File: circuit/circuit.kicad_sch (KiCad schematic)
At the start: 23 parts, among them SW101 SW_Push, SW102 SW_Push, SW103 SW_Push, SW104 SW_Push, SW105 SW_Push, SW106 SW_Push, SW107 SW_Push, SW108 SW_Push, SW109 SW_Push, SW110 SW_Push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

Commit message: Hopefully close to finished
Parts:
- removed U5: ESP32-S3-DevKitC, Esp32 DevKits:ESP32-S3-DevKitC, symbol PCM_Espressif:ESP32-S3-DevKitC
- added U5: ESP32-S3-DevKitC, ESP:ESP32-S3-DevKitC, symbol Espressif:ESP32-S3-DevKitC
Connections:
- net +5V: now also U5.21 (5V)
- net 3.3V: now also U5.1 (3V3), U5.2 (3V3)
- net GND: now also U5.22 (GND), U5.23 (GND), U5.24 (GND), U5.44 (GND)
- net SR_DS: now also U5.9 (GPIO16/ADC2_CH5/32K_N)
- net SR_OE: now also U5.25 (GPIO19/USB_D-)
- net SR_SHCP: now also U5.10 (GPIO17/ADC2_CH6)
- net SR_STCP: now also U5.11 (GPIO18/ADC2_CH7)
- net at C103.2, SW103.1: now also U5.12 (GPIO8/ADC1_CH7)
- net at C105.2, SW105.1: now also U5.16 (GPIO10/ADC1_CH9)
- net at C107.2, SW107.1: now also U5.18 (GPIO12/ADC2_CH1)
- net at Disp101.2 (SDA): now also U5.4 (GPIO4/ADC1_CH3)
- net at Disp101.3 (SCL): now also U5.5 (GPIO5/ADC1_CH4)
- net at C106.2, SW106.1: now also U5.17 (GPIO11/ADC2_CH0)
- net at C109.2, SW109.1: now also U5.20 (GPIO14/ADC2_CH3)
- net at C102.2, SW102.1: now also U5.7 (GPIO7/ADC1_CH6)
- net at C108.2, SW108.1: now also U5.19 (GPIO13/ADC2_CH2)
- net at C110.2, SW110.1: now also U5.8 (GPIO15/ADC2_CH4/32K_P)
- net at C104.2, SW104.1: now also U5.15 (GPIO9/ADC1_CH8)
- net at C101.2, SW101.1: now also U5.6 (GPIO6/ADC1_CH5)
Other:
- sheet IO Routing ports: added none; removed U10_Q[0..5]
- sheet Pedal Routing 1 - 4 ports: added U9_Q[0..7]; removed U7_Q[0..7]
- sheet Pedal Routing 5 - 8 ports: added U10_Q[0..7]; removed U10_Q[0..5], U8_Q[0..7]
- sheet Shift Registers ports: added U10_Q[0..7]; removed U10_Q[0..5]

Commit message: Created pdf and made minor readabilty changes.
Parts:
- C101, C102, C103, C104, C105, C106, C107, C108, C109, C110: value 0.1mF -> .1uF
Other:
- sheet IO Routing: file iorouting.kicad_sch -> io_routing.kicad_sch
- sheet Pedal Routing 5 - 8: file pedal_routing_4-8.kicad_sch -> pedal_routing_5-8.kicad_sch
- title: (none) -> ESP332 Guitar Patch Bay
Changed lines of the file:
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@@
 	(generator "eeschema")
 	(generator_version "9.0")
-	(paper "A2")
+	(paper "USLetter")
+	(title_block
+		(title "ESP332 Guitar Patch Bay")
+		(date "2025-05-27")
+		(rev "1")
+	)
 	(junction
 		(at 349.25 114.3)
@@
 	)
 	(junction
+		(at 375.92 38.1)
+		(diameter 0)
+		(color 0 0 0 0)
+	)
+	(junction
 		(at 386.08 38.1)
 		(diameter 0)
@@
 			)
 		)
-		(property "Value" "0.1mF"
+		(property "Value" ".1uF"
 			(at 330.1936 106.68 90)
 			(effects
@@
 			)
 		)
-		(property "Value" "0.1mF"
+		(property "Value" ".1uF"
 			(at 292.0936 132.08 90)
 			(effects
@@
 			)
 		)
-		(property "Value" "0.1mF"
+		(property "Value" ".1uF"
 			(at 279.3936 119.38 90)
 			(effects
@@
 			)
 		)
-		(property "Value" "0.1mF"
+		(property "Value" ".1uF"
 			(at 304.7936 81.28 90)
 			(effects
@@
 			)
 		)
-		(property "Value" "0.1mF"
+		(property "Value" ".1uF"
 			(at 317.4936 157.48 90)
 			(effects
@@
 			)
 		)
-		(property "Value" "0.1mF"
+		(property "Value" ".1uF"
 			(at 304.7936 144.78 90)
 			(effects
@@
 			)
 		)
-		(property "Value" "0.1mF"
+		(property "Value" ".1uF"
 			(at 330.1936 170.18 90)
 			(effects
@@
 	)
 	(symbol
+		(lib_id "power:PWR_FLAG")
+		(at 375.92 38.1 90)
+		(unit 1)
+		(exclude_from_sim no)
+		(in_bom yes)
+		(on_board yes)
+		(dnp no)
+		(fields_autoplaced yes)
+		(property "Reference" "#FLG0102"
+			(at 374.015 38.1 0)
+			(effects
+				(font
+					(size 1.27 1.27)
+				)
+				(hide yes)
+			)
+		)
+		(property "Value" "GND"
+			(at 372.11 38.0999 90)
+			(effects
+				(font
+					(size 1.27 1.27)
+				)
+				(justify left)
+			)
+		)
+		(property "Footprint" ""
+			(at 375.92 38.1 0)
+			(effects
+				(font
+					(size 1.27 1.27)
+				)
+				(hide yes)
+			)
+		)
+		(property "Datasheet" "~"
+			(at 375.92 38.1 0)
+			(effects
+				(font
+					(size 1.27 1.27)
+				)
+				(hide yes)
+			)
+		)
+		(property "Description" "Special symbol for telling ERC where power comes from"
+			(at 375.92 38.1 0)
+			(effects
+				(font
+					(size 1.27 1.27)
+				)
+				(hide yes)
+			)
+		)
+		(pin "1"
+		)
+		(instances
+			(project "circuit"
+				(path "/420e3d7a-6c9a-4806-b4be-05d56aeb21de"
+					(reference "#FLG0102")
+					(unit 1)
+				)
+			)
+		)
+	)
+	(symbol
 		(lib_id "Device:C_Small")
 		(at 317.5 97.79 270)
@@
 			)
 		)
-		(property "Value" "0.1mF"
+		(property "Value" ".1uF"
 			(at 317.4936 93.98 90)
 			(effects
@@
 			)
 		)
-		(property "Value" "0.1mF"
+		(property "Value" ".1uF"
 			(at 279.3936 55.88 90)
 			(effects
@@
 			)
 		)
-		(property "Value" "0.1mF"
+		(property "Value" ".1uF"
 			(at 292.0936 68.58 90)
 			(effects
@@
 	(symbol
 		(lib_id "power:PWR_FLAG")
-		(at 386.08 38.1 0)
+		(at 386.08 38.1 270)
 		(unit 1)
 		(exclude_from_sim no)
@@
 		(fields_autoplaced yes)
 		(property "Reference" "#FLG0101"
-			(at 386.08 36.195 0)
+			(at 387.985 38.1 0)
 			(effects
 				(font
@@
 		)
 		(property "Value" "AGND"
-			(at 386.08 33.02 0)
+			(at 389.89 38.0999 90)
 			(effects
 				(font
 					(size 1.27 1.27)
 				)
+				(justify left)
 			)
 		)
@@
 			)
 		)
-		(property "Sheetfile" "pedal_routing_4-8.kicad_sch"
+		(property "Sheetfile" "pedal_routing_5-8.kicad_sch"
 			(at 237.49 348.5646 0)
 			(effects
@@
 			)
 		)
-		(property "Sheetfile" "iorouting.kicad_sch"
+		(property "Sheetfile" "io_routing.kicad_sch"
 			(at 237.49 227.9146 0)
 			(effects

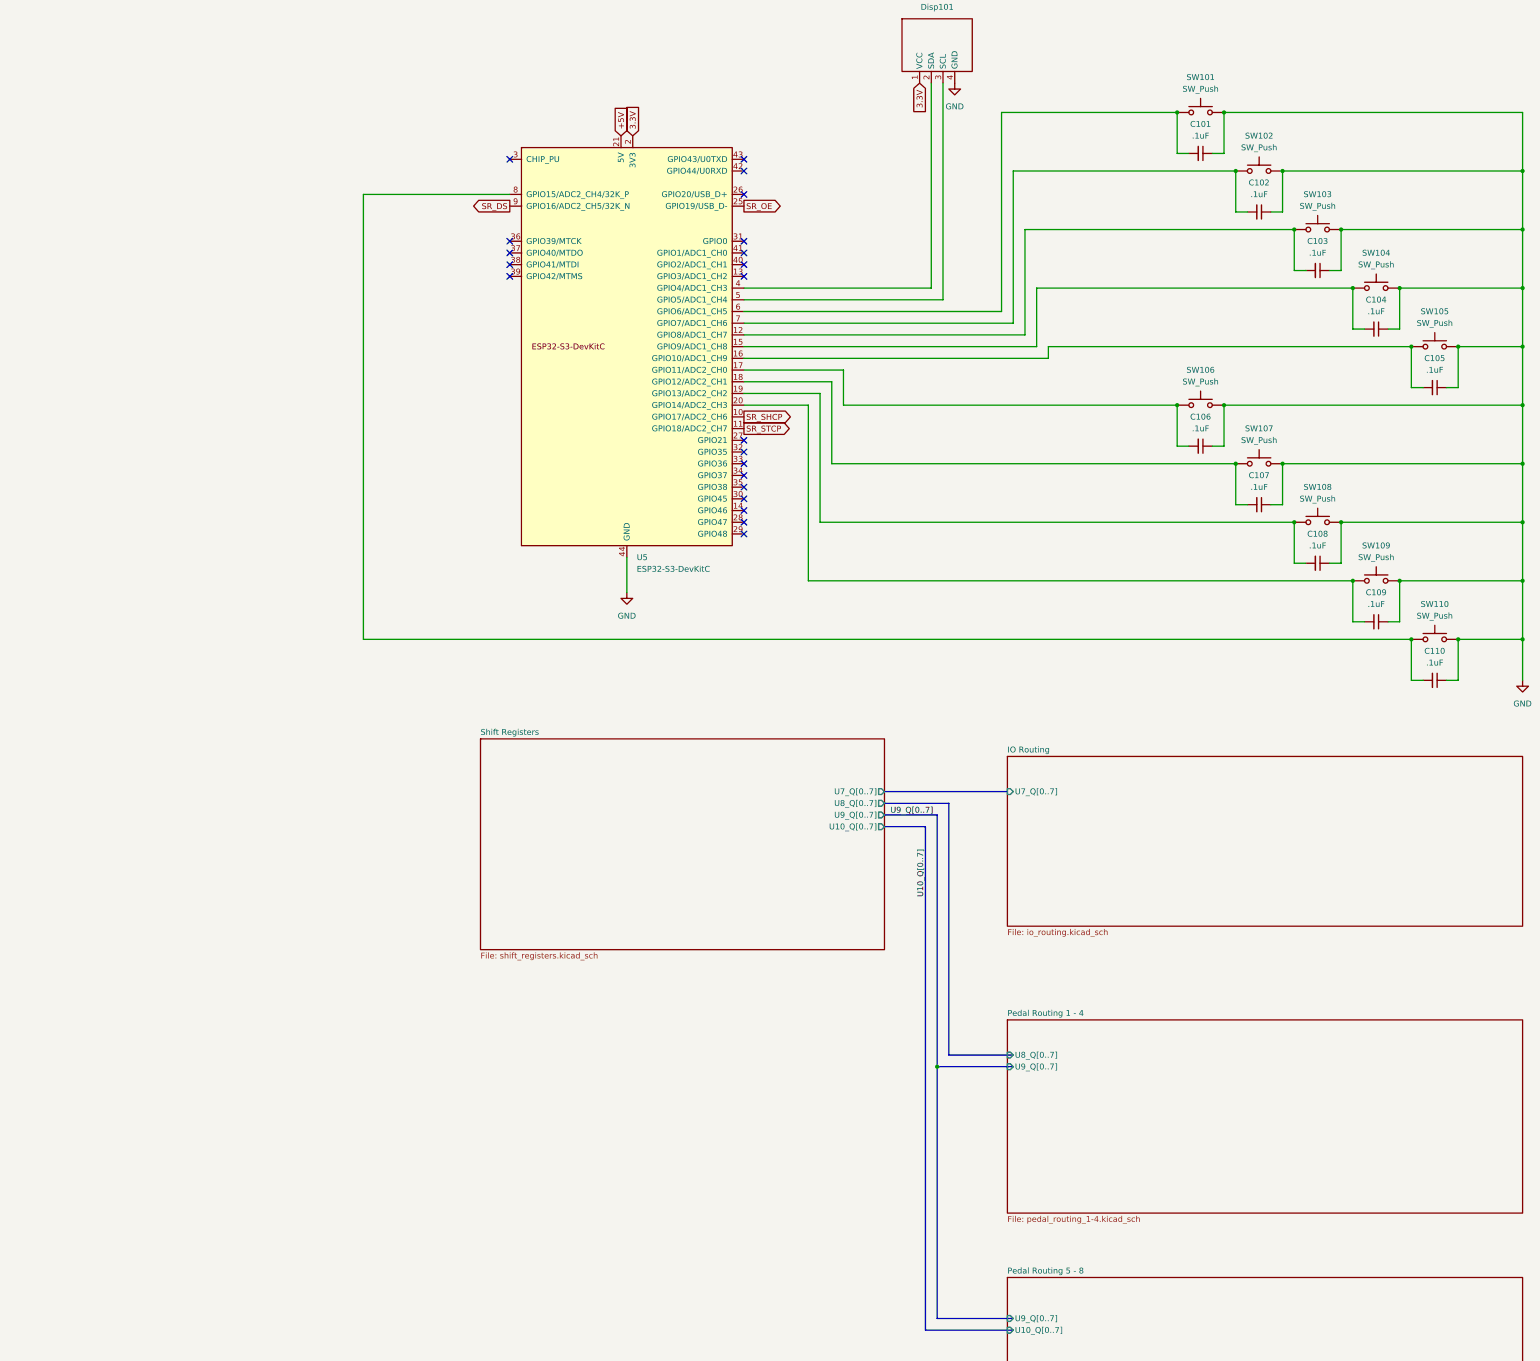
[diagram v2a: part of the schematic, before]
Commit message: Added LEDs and shift registers
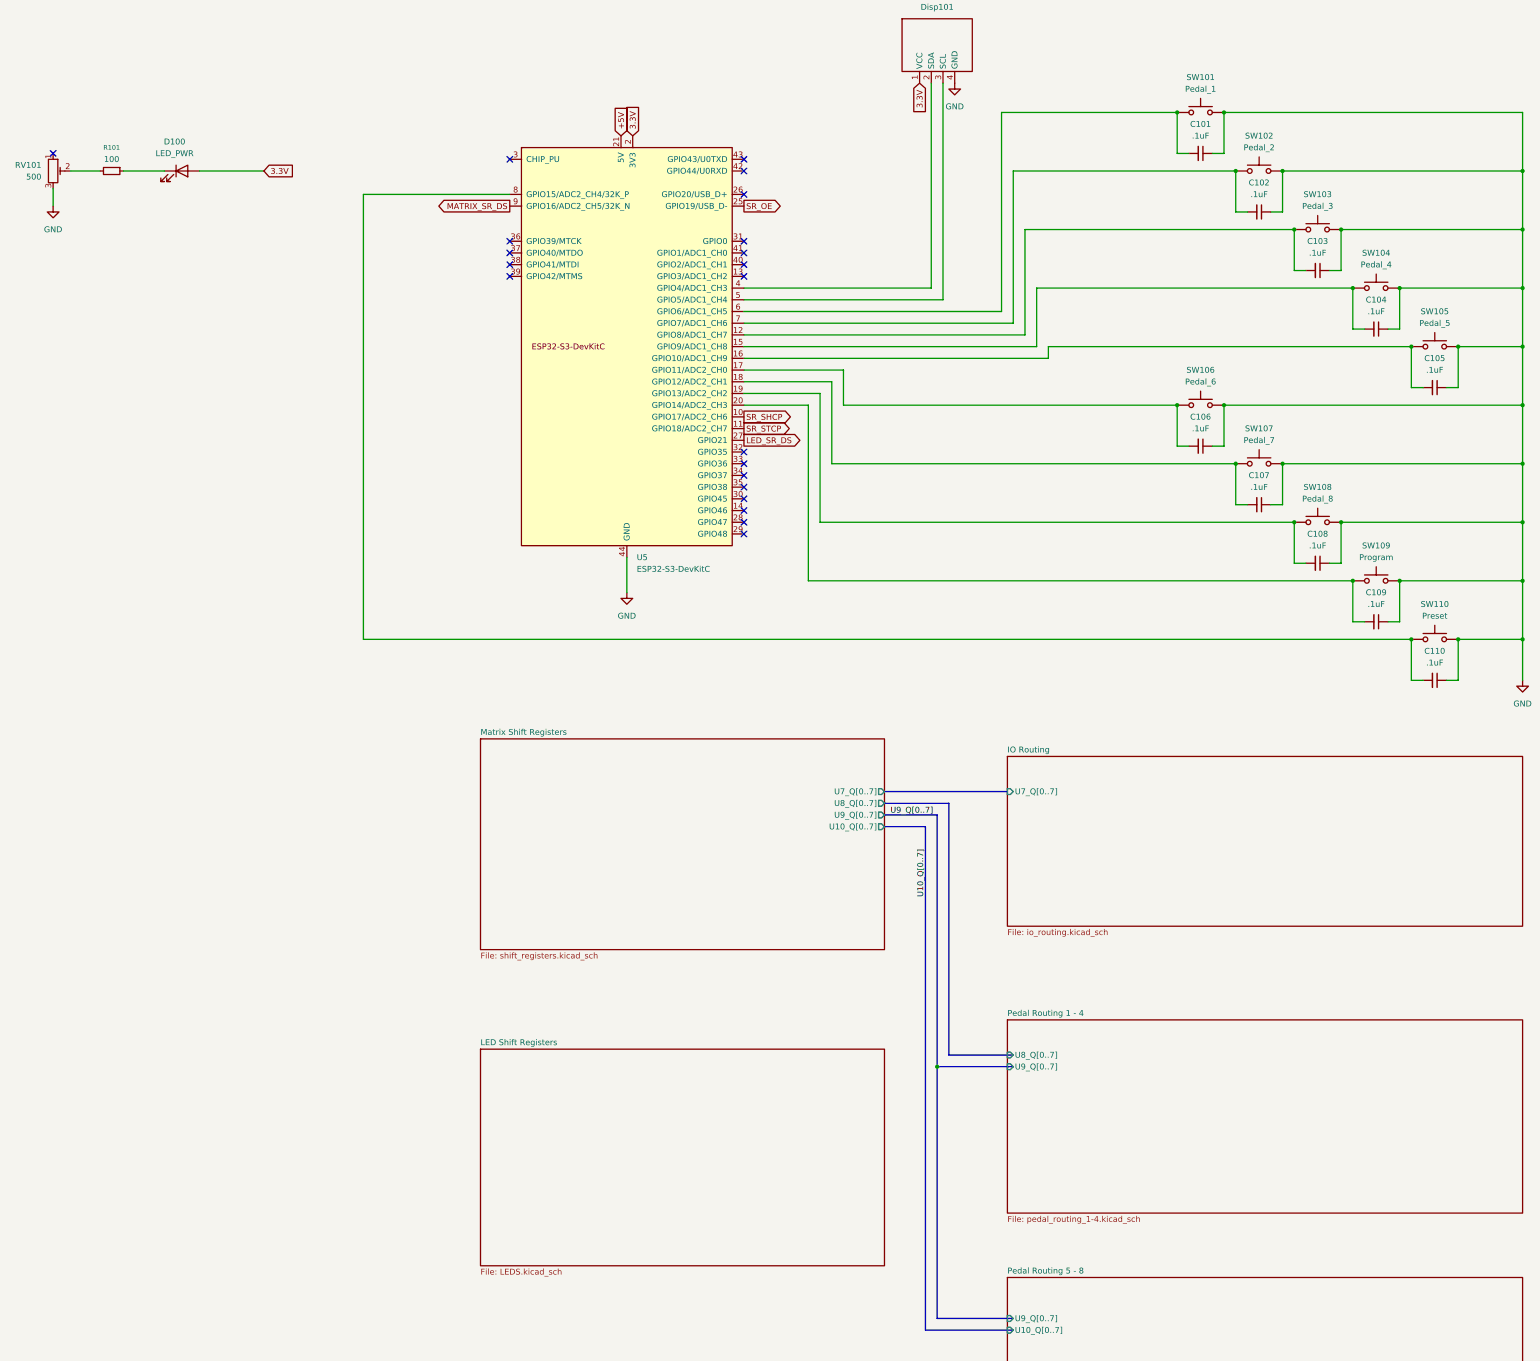
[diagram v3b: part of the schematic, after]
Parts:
- added D100: LED_PWR, Connector_Wire:SolderWire-0.1sqmm_1x02_P3.6mm_D0.4mm_OD1mm, symbol Device:LED
- added R101: 100, Resistor_THT:R_Axial_DIN0204_L3.6mm_D1.6mm_P5.08mm_Horizontal, symbol Device:R_Small
- added RV101: 500, Potentiometer_THT:Potentiometer_Bourns_3339P_Vertical, symbol Device:R_Potentiometer_Trim
- SW101: value SW_Push -> Pedal_1
- SW102: value SW_Push -> Pedal_2
- SW103: value SW_Push -> Pedal_3
- SW104: value SW_Push -> Pedal_4
- SW105: value SW_Push -> Pedal_5
- SW106: value SW_Push -> Pedal_6
- SW107: value SW_Push -> Pedal_7
- SW108: value SW_Push -> Pedal_8
- SW109: value SW_Push -> Program
- SW110: value SW_Push -> Preset
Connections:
- net 3.3V: now also D100.2 (A)
- net GND: now also RV101.3
- net LED_SR_DS: now reaches U5.27 (GPIO21)
- net SR_DS renamed MATRIX_SR_DS
- new net: D100.1 (K), R101.1
- new net: R101.2, RV101.2
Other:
- sheet Shift Registers renamed Matrix Shift Registers
- added sheet LED Shift Registers (LEDS.kicad_sch)

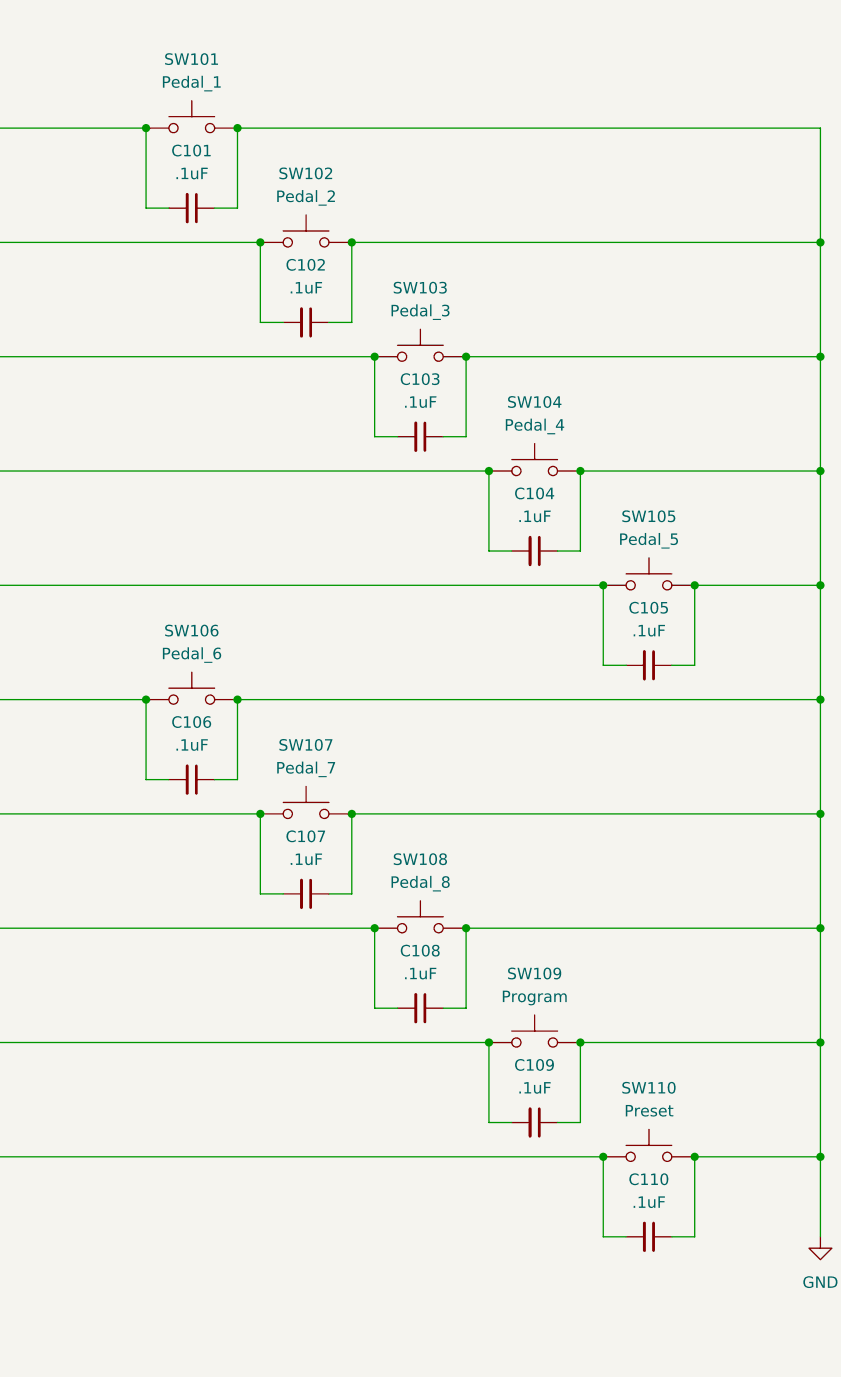
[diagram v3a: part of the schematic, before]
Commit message: Very tentative PCB layout, Code compiles but needs major functionality testing.
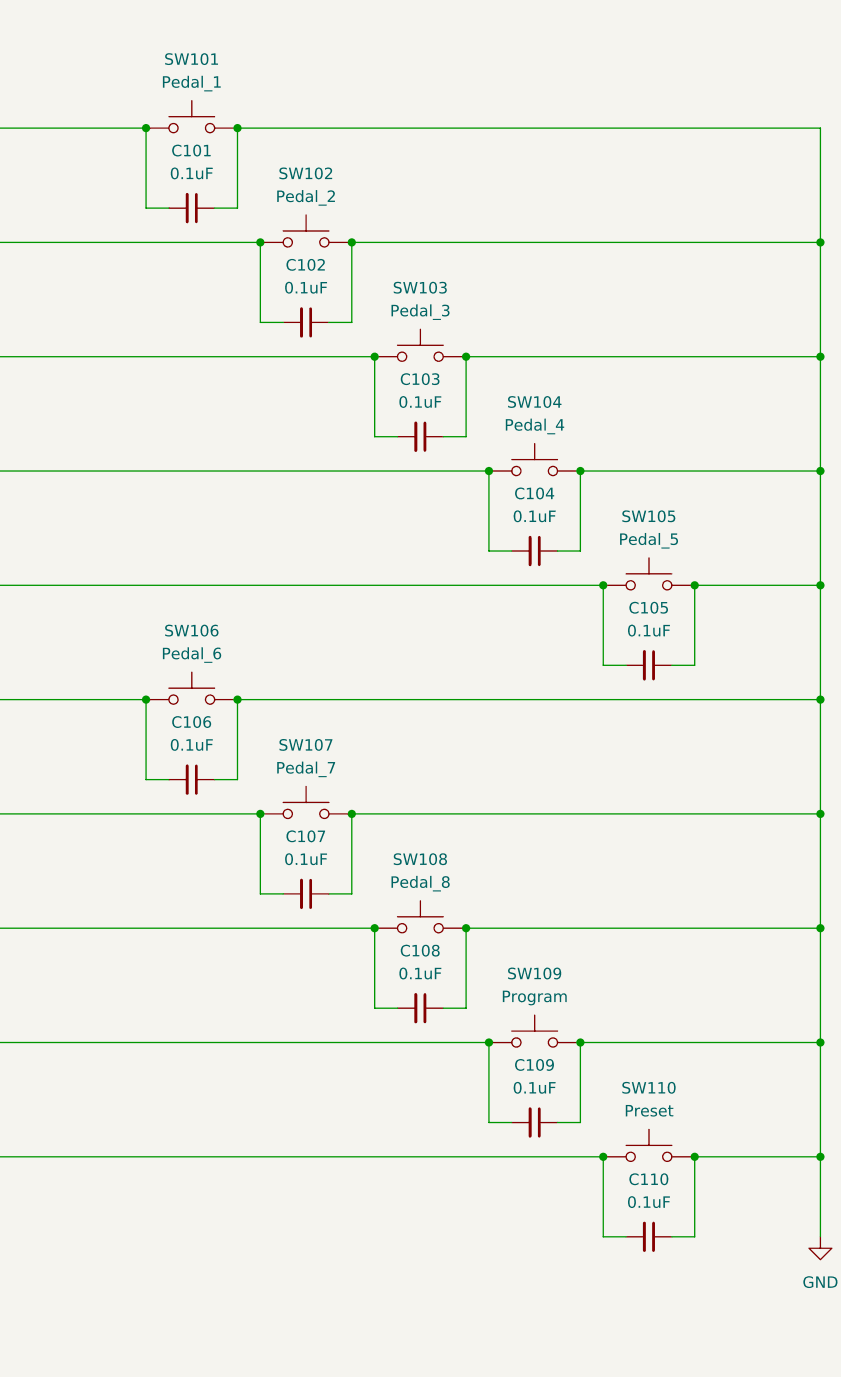
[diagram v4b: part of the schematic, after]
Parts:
- C101, C102, C103, C104, C105, C106, C107, C108, C109, C110: value .1uF -> 0.1uF
- Disp101: footprint Connector_Wire:SolderWire-1.5sqmm_1x04_P6mm_D1.7mm_OD3mm -> Connector_PinHeader_1.00mm:PinHeader_1x04_P1.00mm_Vertical
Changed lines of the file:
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@@
 			)
 		)
-		(property "Value" ".1uF"
+		(property "Value" "0.1uF"
 			(at 330.1936 106.68 90)
 			(effects
@@
 			)
 		)
-		(property "Value" ".1uF"
+		(property "Value" "0.1uF"
 			(at 292.0936 132.08 90)
 			(effects
@@
 			)
 		)
-		(property "Footprint" "Connector_Wire:SolderWire-1.5sqmm_1x04_P6mm_D1.7mm_OD3mm"
+		(property "Footprint" "Connector_PinHeader_1.00mm:PinHeader_1x04_P1.00mm_Vertical"
 			(at 222.25 35.56 0)
 			(effects
@@
 			)
 		)
-		(property "Value" ".1uF"
+		(property "Value" "0.1uF"
 			(at 279.3936 119.38 90)
 			(effects
@@
 			)
 		)
-		(property "Value" ".1uF"
+		(property "Value" "0.1uF"
 			(at 304.7936 81.28 90)
 			(effects
@@
 			)
 		)
-		(property "Value" ".1uF"
+		(property "Value" "0.1uF"
 			(at 317.4936 157.48 90)
 			(effects
@@
 			)
 		)
-		(property "Value" ".1uF"
+		(property "Value" "0.1uF"
 			(at 304.7936 144.78 90)
 			(effects
@@
 			)
 		)
-		(property "Value" ".1uF"
+		(property "Value" "0.1uF"
 			(at 330.1936 170.18 90)
 			(effects
@@
 			)
 		)
-		(property "Value" ".1uF"
+		(property "Value" "0.1uF"
 			(at 317.4936 93.98 90)
 			(effects
@@
 			)
 		)
-		(property "Value" ".1uF"
+		(property "Value" "0.1uF"
 			(at 279.3936 55.88 90)
 			(effects
@@
 			)
 		)
-		(property "Value" ".1uF"
+		(property "Value" "0.1uF"
 			(at 292.0936 68.58 90)
 			(effects
